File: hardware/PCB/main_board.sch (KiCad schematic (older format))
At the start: 4 parts

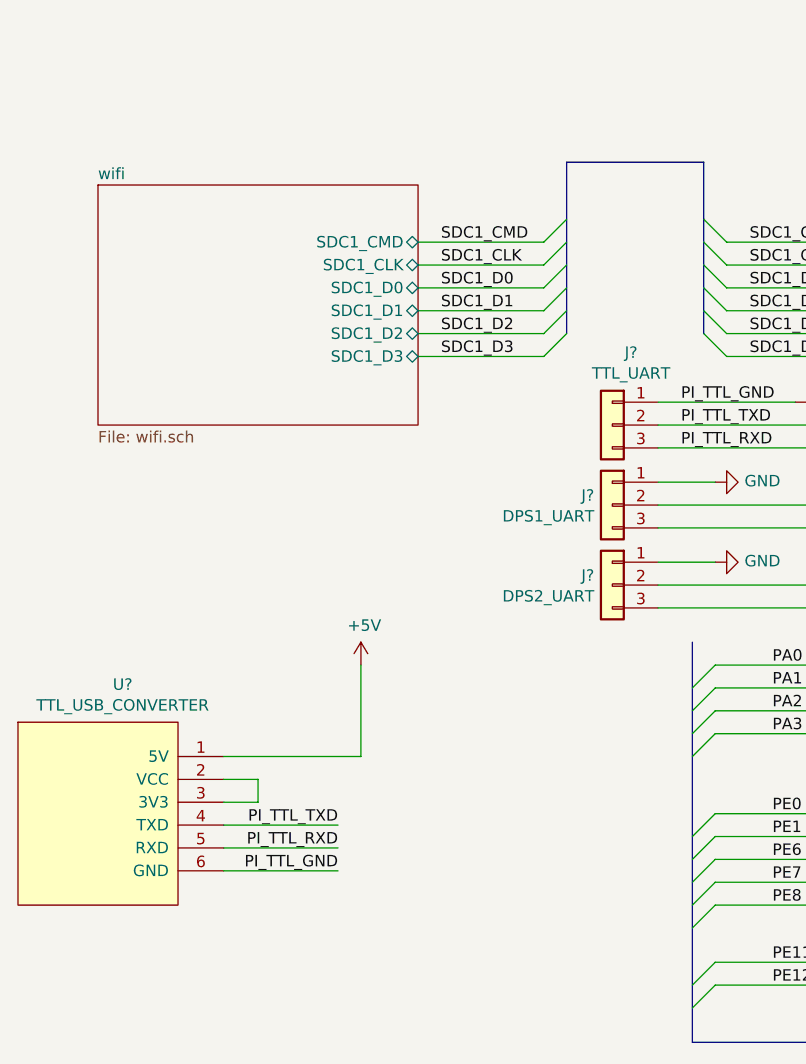
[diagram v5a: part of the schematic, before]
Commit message: update rtl8723 circuit,
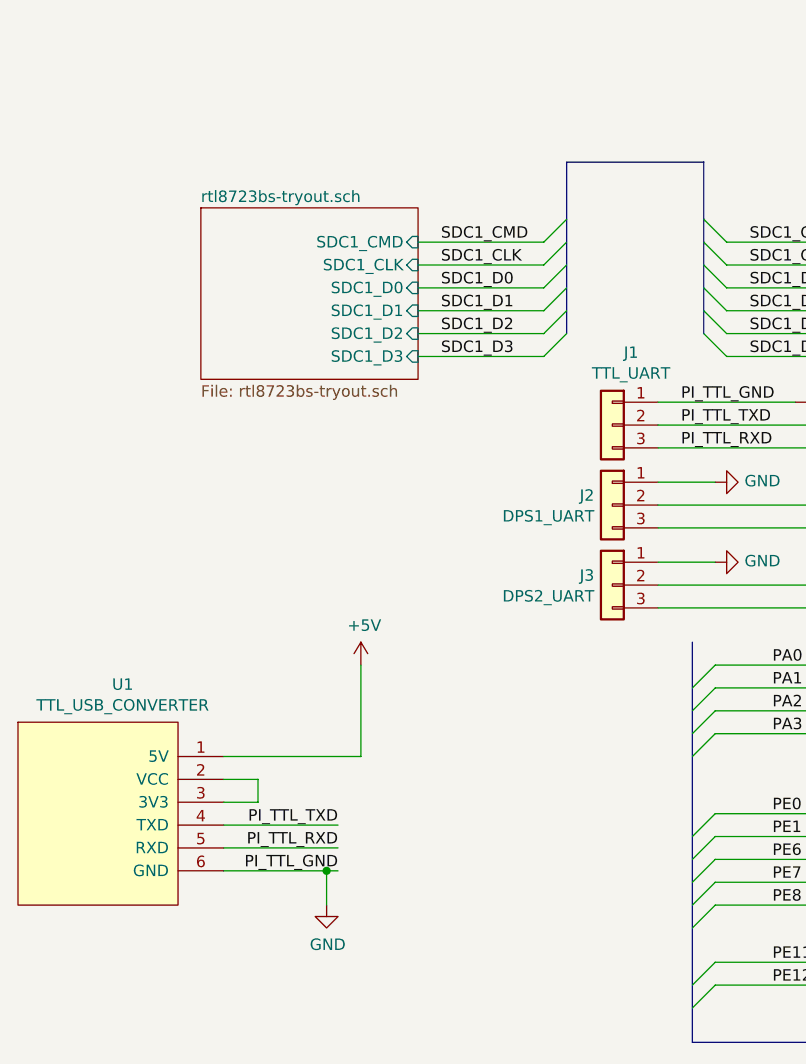
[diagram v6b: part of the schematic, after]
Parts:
- J1, J2, J3: renamed from J?; footprint (none) -> Connector_PinHeader_2.54mm:PinHeader_1x04_P2.54mm_Vertical
- gave numbers to parts that had none: 1
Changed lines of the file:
@@
 Wire Wire Line
 	2900 3050 3450 3050
-$Sheet
-S 1500 2400 1400 1050
-U 5E8B2717
-F0 "wifi" 50
-F1 "wifi.sch" 50
-F2 "SDC1_D2" B R 2900 3050 50
-F3 "SDC1_D1" B R 2900 2950 50
-F4 "SDC1_D0" B R 2900 2850 50
-F5 "SDC1_CLK" B R 2900 2750 50
-F6 "SDC1_CMD" B R 2900 2650 50
-F7 "SDC1_D3" B R 2900 3150 50
-$EndSheet
 Text Label 3000 2650 0    50   ~ 0
 SDC1_CMD
@@
 	7050 3900 7650 3900
 $Comp
-L Connector_Generic:Conn_01x03 J?
+L Connector_Generic:Conn_01x03 J1
 U 1 1 5E949A7D
 P 3750 3450
-F 0 "J?" H 3668 3767 50  0000 C CNN
+F 0 "J1" H 3668 3767 50  0000 C CNN
 F 1 "TTL_UART" H 3668 3676 50  0000 C CNN
-F 2 "" H 3750 3450 50  0001 C CNN
+F 2 "Connector_PinHeader_2.54mm:PinHeader_1x04_P2.54mm_Vertical" H 3750 3450 50  0001 C CNN
 F 3 "~" H 3750 3450 50  0001 C CNN
 	1    3750 3450
@@
 	3950 3550 4800 3550
 $Comp
-L Connector_Generic:Conn_01x03 J?
+L Connector_Generic:Conn_01x03 J2
 U 1 1 5E94B27C
 P 3750 3800
-F 0 "J?" H 3829 3842 50  0000 L CNN
+F 0 "J2" H 3829 3842 50  0000 L CNN
 F 1 "DPS1_UART" H 3829 3751 50  0000 L CNN
-F 2 "" H 3750 3800 50  0001 C CNN
+F 2 "Connector_PinHeader_2.54mm:PinHeader_1x04_P2.54mm_Vertical" H 3750 3800 50  0001 C CNN
 F 3 "~" H 3750 3800 50  0001 C CNN
 	1    3750 3800
@@
 $EndComp
 $Comp
-L power:GND #PWR?
+L power:GND #PWR0101
 U 1 1 5E94B286
 P 4200 3700
-F 0 "#PWR?" H 4200 3450 50  0001 C CNN
+F 0 "#PWR0101" H 4200 3450 50  0001 C CNN
 F 1 "GND" V 4205 3572 50  0000 R CNN
 F 2 "" H 4200 3700 50  0001 C CNN
@@
 	3950 3900 4800 3900
 $Comp
-L Connector_Generic:Conn_01x03 J?
+L Connector_Generic:Conn_01x03 J3
 U 1 1 5E94C724
 P 3750 4150
-F 0 "J?" H 3829 4192 50  0000 L CNN
+F 0 "J3" H 3829 4192 50  0000 L CNN
 F 1 "DPS2_UART" H 3829 4101 50  0000 L CNN
-F 2 "" H 3750 4150 50  0001 C CNN
+F 2 "Connector_PinHeader_2.54mm:PinHeader_1x04_P2.54mm_Vertical" H 3750 4150 50  0001 C CNN
 F 3 "~" H 3750 4150 50  0001 C CNN
 	1    3750 4150
@@
 $EndComp
 $Comp
-L power:GND #PWR?
+L power:GND #PWR0102
 U 1 1 5E94C72E
 P 4200 4050
-F 0 "#PWR?" H 4200 3800 50  0001 C CNN
+F 0 "#PWR0102" H 4200 3800 50  0001 C CNN
 F 1 "GND" V 4205 3922 50  0000 R CNN
 F 2 "" H 4200 4050 50  0001 C CNN
@@
 	3950 3350 4550 3350
 $Comp
-L power:GND #PWR?
+L power:GND #PWR0131
 U 1 1 5E94A27E
 P 4550 3350
-F 0 "#PWR?" H 4550 3100 50  0001 C CNN
+F 0 "#PWR0131" H 4550 3100 50  0001 C CNN
 F 1 "GND" V 4555 3222 50  0000 R CNN
 F 2 "" H 4550 3350 50  0001 C CNN
@@
 $EndComp
 $Comp
-L taobao-components:TTL_USB_CONVERTER U?
+L taobao-components:TTL_USB_CONVERTER U1
 U 1 1 5E991FE4
 P 1500 5150
-F 0 "U?" H 1608 5715 50  0000 C CNN
+F 0 "U1" H 1608 5715 50  0000 C CNN
 F 1 "TTL_USB_CONVERTER" H 1608 5624 50  0000 C CNN
 F 2 "footprint-lib:TTL_USB_CONVERTER" H 1500 5150 50  0001 C CNN
@@
 	2050 5300 2550 5300
 Wire Wire Line
-	2050 5400 2550 5400
-$Comp
-L customized_power:+5V #PWR?
+	2050 5400 2500 5400
+$Comp
+L customized_power:+5V #PWR0132
 U 1 1 5E99CA17
 P 2650 4500
-F 0 "#PWR?" H 2650 4350 50  0001 C CNN
+F 0 "#PWR0132" H 2650 4350 50  0001 C CNN
 F 1 "+5V" H 2665 4673 50  0000 C CNN
 F 2 "" H 2650 4500 50  0001 C CNN
@@
 	8900 4450 9000 4350
 $Comp
-L power:GND #PWR?
+L power:GND #PWR0133
 U 1 1 5EAAA76D
 P 9350 4950
-F 0 "#PWR?" H 9350 4700 50  0001 C CNN
+F 0 "#PWR0133" H 9350 4700 50  0001 C CNN
 F 1 "GND" H 9355 4777 50  0000 C CNN
 F 2 "" H 9350 4950 50  0001 C CNN
@@
 PE12
 $Comp
-L customized_power:+5V #PWR?
+L customized_power:+5V #PWR0134
 U 1 1 5EB55BB0
 P 9200 1250
-F 0 "#PWR?" H 9200 1100 50  0001 C CNN
+F 0 "#PWR0134" H 9200 1100 50  0001 C CNN
 F 1 "+5V" V 9215 1378 50  0000 L CNN
 F 2 "" H 9200 1250 50  0001 C CNN
@@
 $EndComp
 $Comp
-L customized_power:+3V3 #PWR?
+L customized_power:+3V3 #PWR0135
 U 1 1 5EB55F01
 P 9200 1350
-F 0 "#PWR?" H 9200 1200 50  0001 C CNN
+F 0 "#PWR0135" H 9200 1200 50  0001 C CNN
 F 1 "+3V3" V 9215 1478 50  0000 L CNN
 F 2 "" H 9200 1350 50  0001 C CNN
@@
 Text Label 7500 5800 2    50   ~ 0
 USB_DP
+$Comp
+L power:GND #PWR0137
+U 1 1 5EA4872A
+P 2500 5550
+F 0 "#PWR0137" H 2500 5300 50  0001 C CNN
+F 1 "GND" H 2505 5377 50  0000 C CNN
+F 2 "" H 2500 5550 50  0001 C CNN
+F 3 "" H 2500 5550 50  0001 C CNN
+	1    2500 5550
+	1    0    0    -1
+$EndComp
+Wire Wire Line
+	2500 5550 2500 5400
+Connection ~ 2500 5400
+Wire Wire Line
+	2500 5400 2550 5400
+$Sheet
+S 1950 2500 950  750
+U 5EA427D8
+F0 "rtl8723bs-tryout.sch" 50
+F1 "rtl8723bs-tryout.sch" 50
+F2 "SDC1_D0" I R 2900 2850 50
+F3 "SDC1_D1" I R 2900 2950 50
+F4 "SDC1_D2" I R 2900 3050 50
+F5 "SDC1_D3" I R 2900 3150 50
+F6 "SDC1_CLK" I R 2900 2750 50
+F7 "SDC1_CMD" I R 2900 2650 50
+$EndSheet
 Wire Bus Line
 	3550 2300 3550 3050
